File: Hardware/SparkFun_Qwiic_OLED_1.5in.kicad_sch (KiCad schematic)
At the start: 39 parts, among them J1 Qwiic_RA, J2 Qwiic_RA, J3 Conn_01x06, U1 OLED_1.5in, U5 AP3012

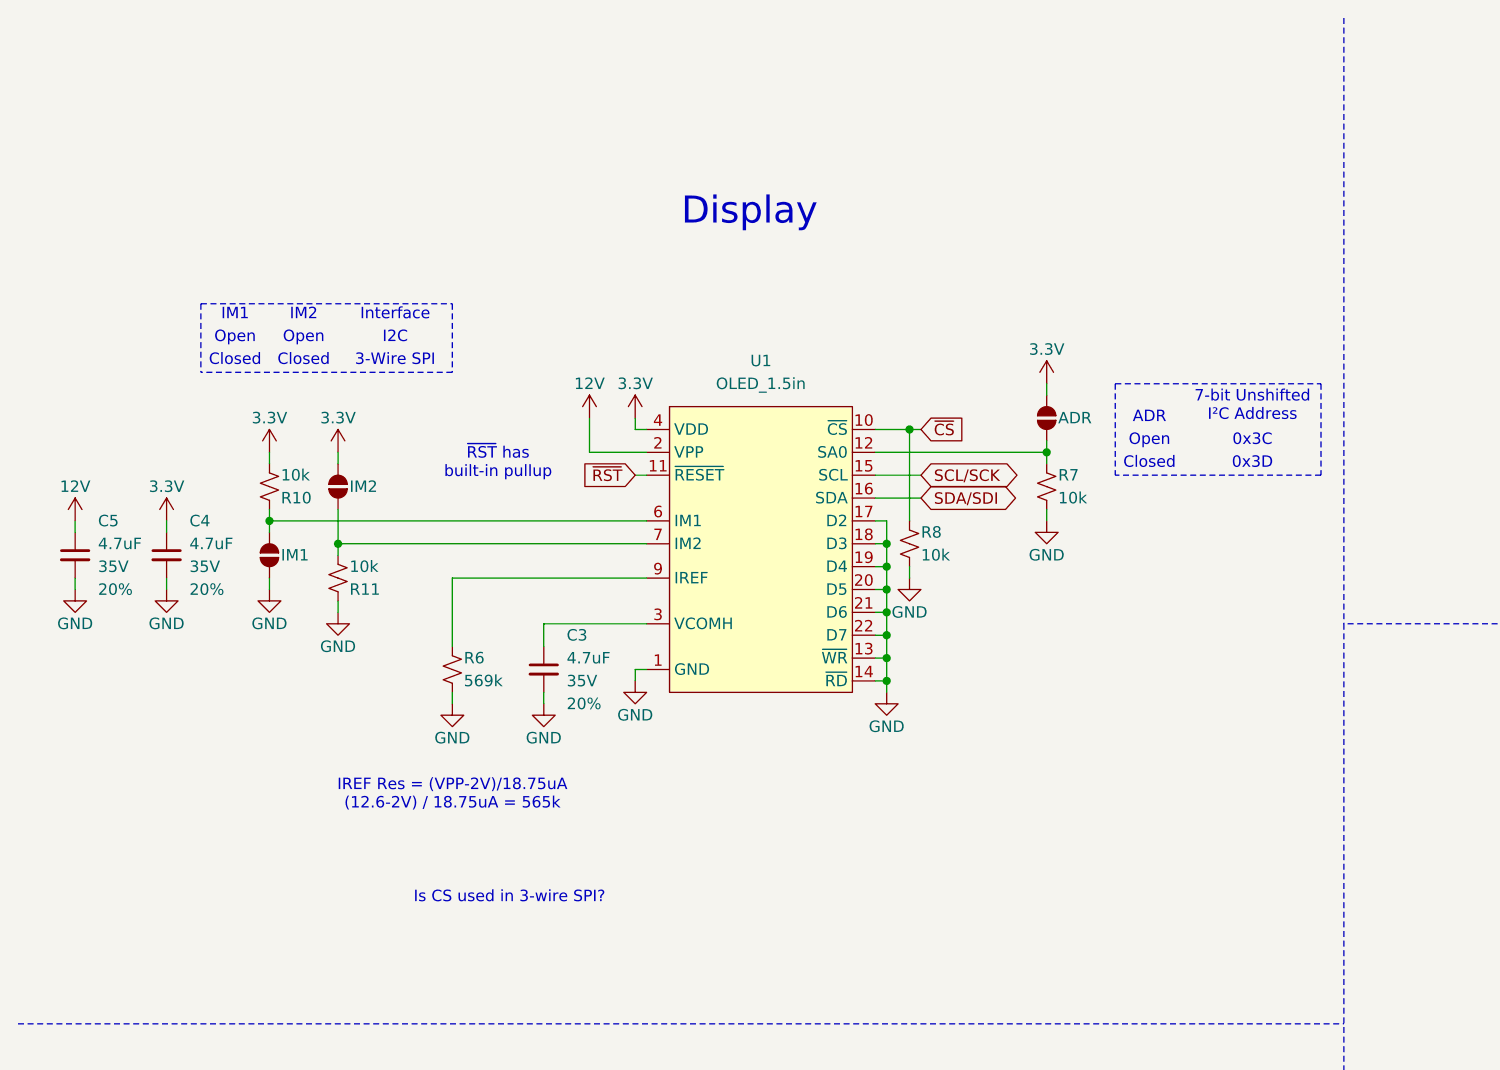
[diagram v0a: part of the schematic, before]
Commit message: Updates the display part to be it's own symbol
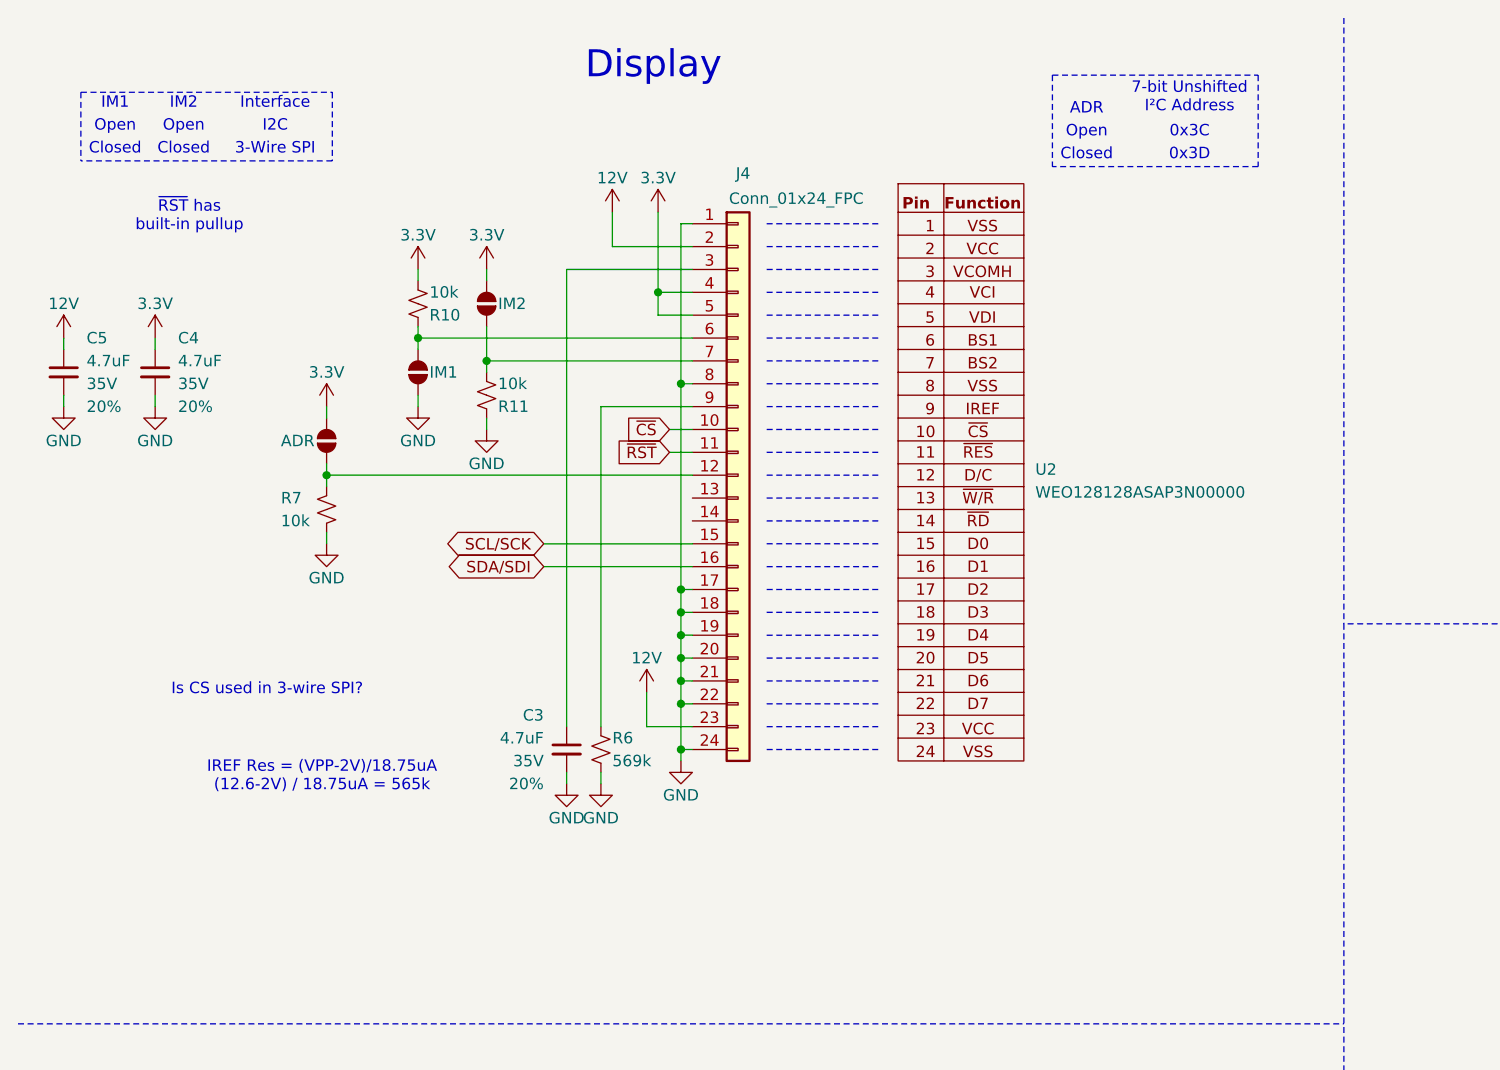
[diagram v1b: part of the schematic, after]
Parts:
- removed R8: 10k, SparkFun-Resistor:R_0603_1608Metric, symbol SparkFun-Resistor:10k_0603
- removed U1: OLED_1.5in, SparkFun-Display:OLED_1.5in_128x128-Folded, symbol SparkFun-Display:OLED_1.5in
- added J4: Conn_01x24_FPC, SparkFun-Connector:FPC_0.5mm-24, symbol SparkFun-Connector:Conn_01x24_FPC_0.5mm
- added U2: WEO128128ASAP3N00000, SparkFun-Display:OLED_1.5in_128x128-Folded, symbol SparkFun-Display:OLED_1.5in_New
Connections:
- net 12V: now also J4.2 (Pin_2), J4.23 (Pin_23)
- net 3.3V: now also J4.4 (Pin_4), J4.5 (Pin_5)
- net SCL/SCK: now also J4.15 (Pin_15)
- net SDA/SDI: now also J4.16 (Pin_16)
- net ~{CS}: now also J4.10 (Pin_10)
- net ~{RST}: now also J4.11 (Pin_11)
- net at JP6.2 (B), R10.2: now also J4.6 (Pin_6)
- net at R6.2: now also J4.9 (Pin_9)
- net at C3.1: now also J4.3 (Pin_3)
- net at JP3.1 (A), R7.2: now also J4.12 (Pin_12)
- net at JP7.1 (A), R11.1: now also J4.7 (Pin_7)
- net ESD_GND renamed GND
- net GND: now also J4.1 (Pin_1), J4.17 (Pin_17), J4.18 (Pin_18), J4.19 (Pin_19), J4.20 (Pin_20), J4.21 (Pin_21), J4.22 (Pin_22), J4.24 (Pin_24), J4.8 (Pin_8)
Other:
- moved on the sheet: C3, C4, C5, R10, R11, R6, R7

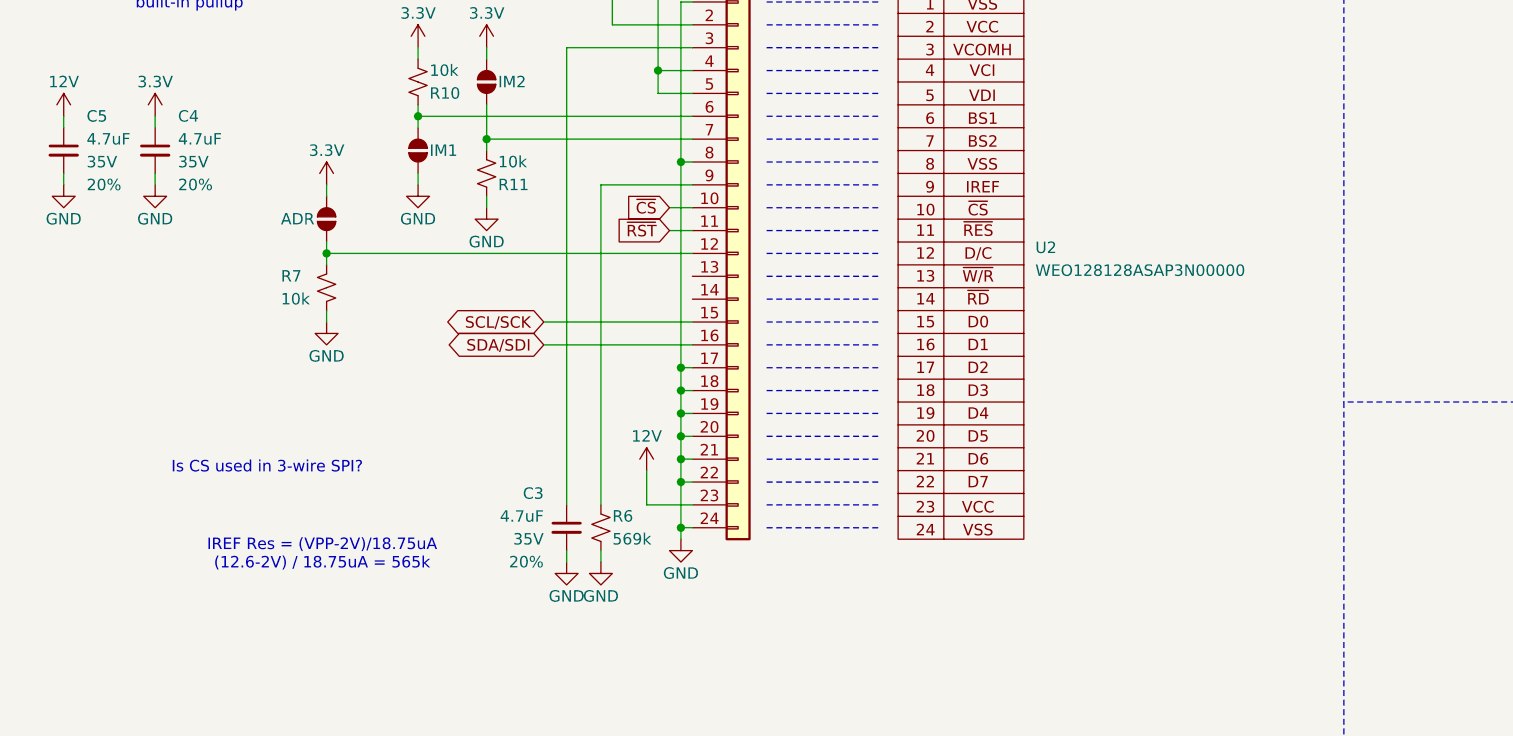
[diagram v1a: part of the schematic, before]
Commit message: Removes connector from OLED symbol
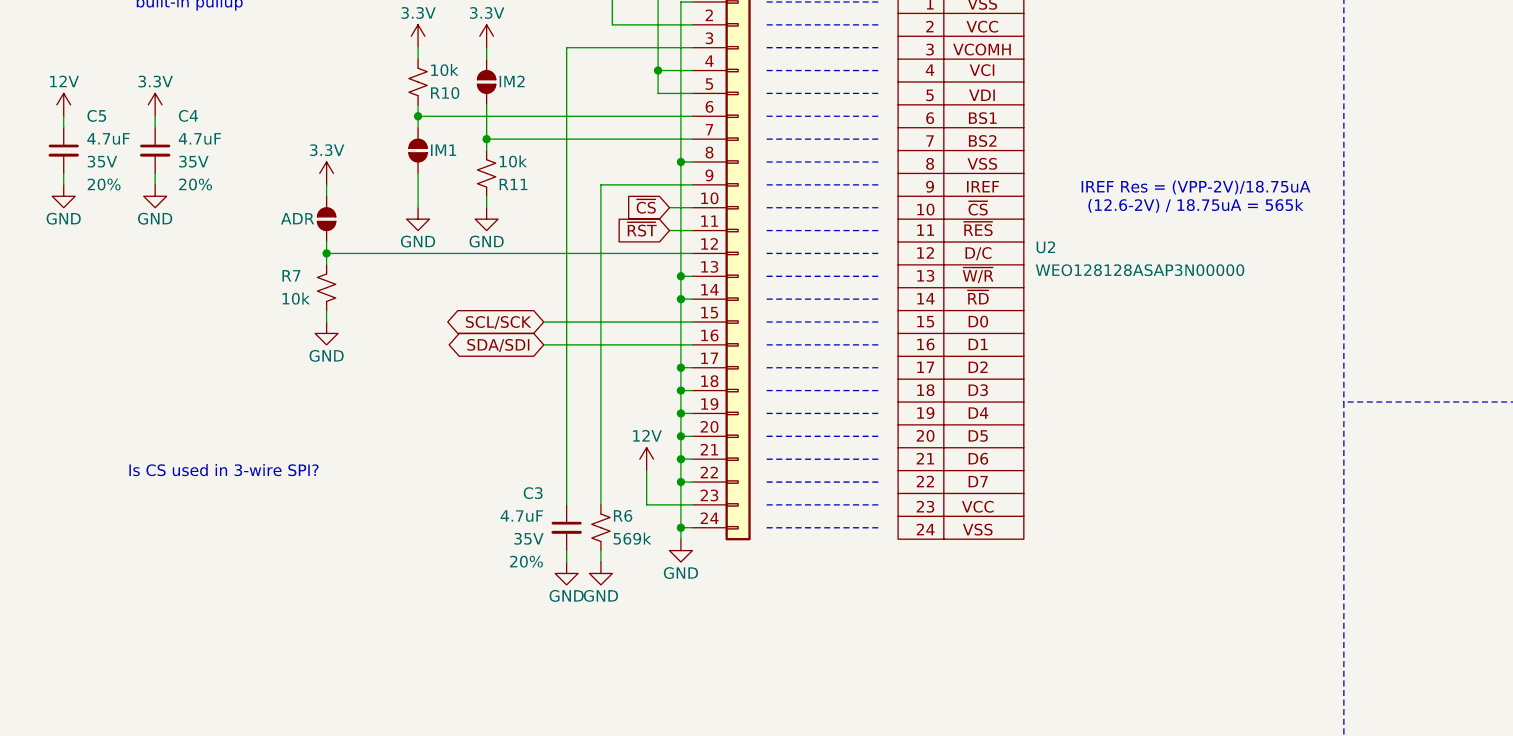
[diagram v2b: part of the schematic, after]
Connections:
- net GND: now also J4.13 (Pin_13), J4.14 (Pin_14)
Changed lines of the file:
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@@
 	(text "IREF Res = (VPP-2V)/18.75uA\n(12.6-2V) / 18.75uA = 565k"
 		(exclude_from_sim no)
-		(at 46.482 98.298 0)
+		(at 143.51 58.674 0)
 		(effects
 			(font
@@
 	(text "Is CS used in 3-wire SPI?"
 		(exclude_from_sim no)
-		(at 40.386 88.646 0)
+		(at 35.56 89.154 0)
 		(effects
 			(font
@@
 	)
 	(junction
+		(at 86.36 69.85)
+		(diameter 0)
+		(color 0 0 0 0)
+	)
+	(junction
 		(at 83.82 44.45)
 		(diameter 0)
@@
 	)
 	(junction
+		(at 86.36 67.31)
+		(diameter 0)
+		(color 0 0 0 0)
+	)
+	(junction
 		(at 46.99 64.77)
 		(diameter 0)
@@
 	(wire
 		(pts
+			(xy 86.36 67.31) (xy 86.36 69.85)
+		)
+		(stroke
+			(width 0)
+			(type default)
+		)
+	)
+	(wire
+		(pts
 			(xy 85.09 173.99) (xy 83.82 173.99)
 		)
@@
 		)
 	)
+	(wire
+		(pts
+			(xy 86.36 67.31) (xy 87.63 67.31)
+		)
+		(stroke
+			(width 0)
+			(type default)
+		)
+	)
 	(polyline
 		(pts
@@
 	(wire
 		(pts
+			(xy 86.36 69.85) (xy 87.63 69.85)
+		)
+		(stroke
+			(width 0)
+			(type default)
+		)
+	)
+	(wire
+		(pts
 			(xy 83.82 176.53) (xy 83.82 177.8)
 		)
@@
 	(wire
 		(pts
+			(xy 86.36 69.85) (xy 86.36 77.47)
+		)
+		(stroke
+			(width 0)
+			(type default)
+		)
+	)
+	(wire
+		(pts
 			(xy 57.15 48.26) (xy 57.15 49.53)
 		)
@@
 	(wire
 		(pts
-			(xy 57.15 57.15) (xy 57.15 55.88)
+			(xy 57.15 59.69) (xy 57.15 55.88)
 		)
 		(stroke
@@
 	(wire
 		(pts
-			(xy 86.36 54.61) (xy 86.36 77.47)
+			(xy 86.36 54.61) (xy 86.36 67.31)
 		)
 		(stroke
@@
 	(symbol
 		(lib_id "SparkFun-PowerSymbol:GND")
-		(at 57.15 57.15 0)
+		(at 57.15 59.69 0)
 		(unit 1)
 		(exclude_from_sim no)
@@
 		(fields_autoplaced yes)
 		(property "Reference" "#PWR02"
-			(at 57.15 63.5 0)
+			(at 57.15 66.04 0)
 			(effects
 				(font
@@
 		)
 		(property "Value" "GND"
-			(at 57.15 60.96 0)
+			(at 57.15 63.5 0)
 			(do_not_autoplace yes)
 			(effects
@@
 		)
 		(property "Footprint" ""
-			(at 57.15 57.15 0)
+			(at 57.15 59.69 0)
 			(effects
 				(font
@@
 		)
 		(property "Datasheet" ""
-			(at 57.15 57.15 0)
+			(at 57.15 59.69 0)
 			(effects
 				(font
@@
 		)
 		(property "Description" "Power symbol creates a global label with name \"GND\" , ground"
-			(at 57.15 66.04 0)
+			(at 57.15 68.58 0)
 			(effects
 				(font

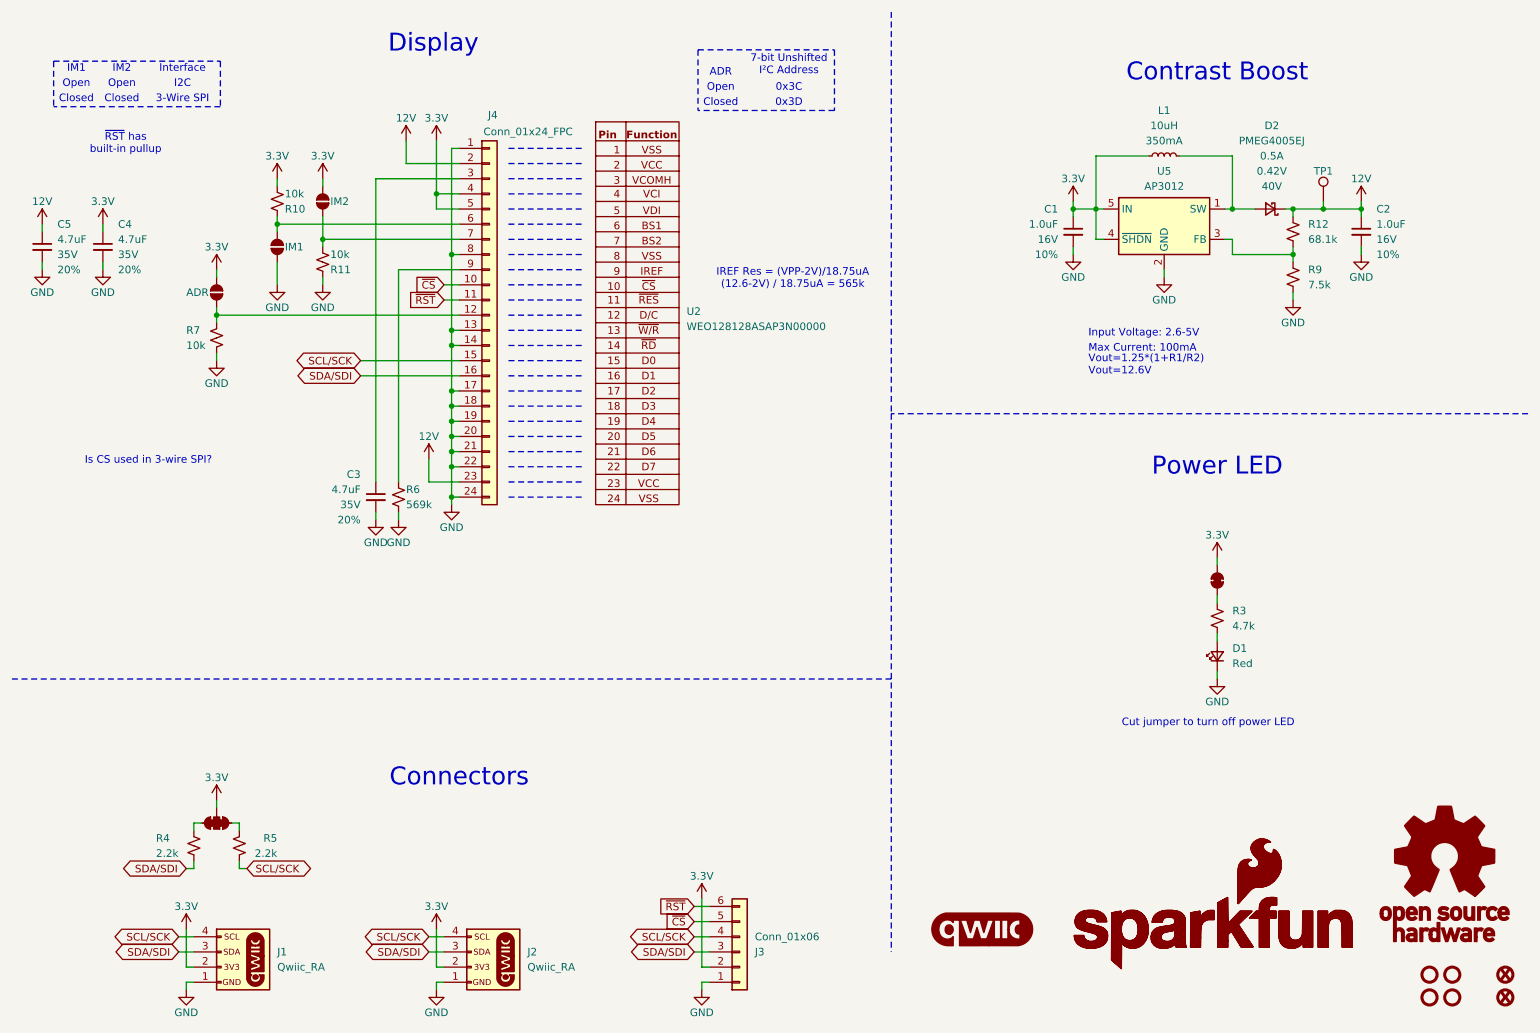
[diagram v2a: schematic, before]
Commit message: Removes connector from OLED symbolbol and footprint
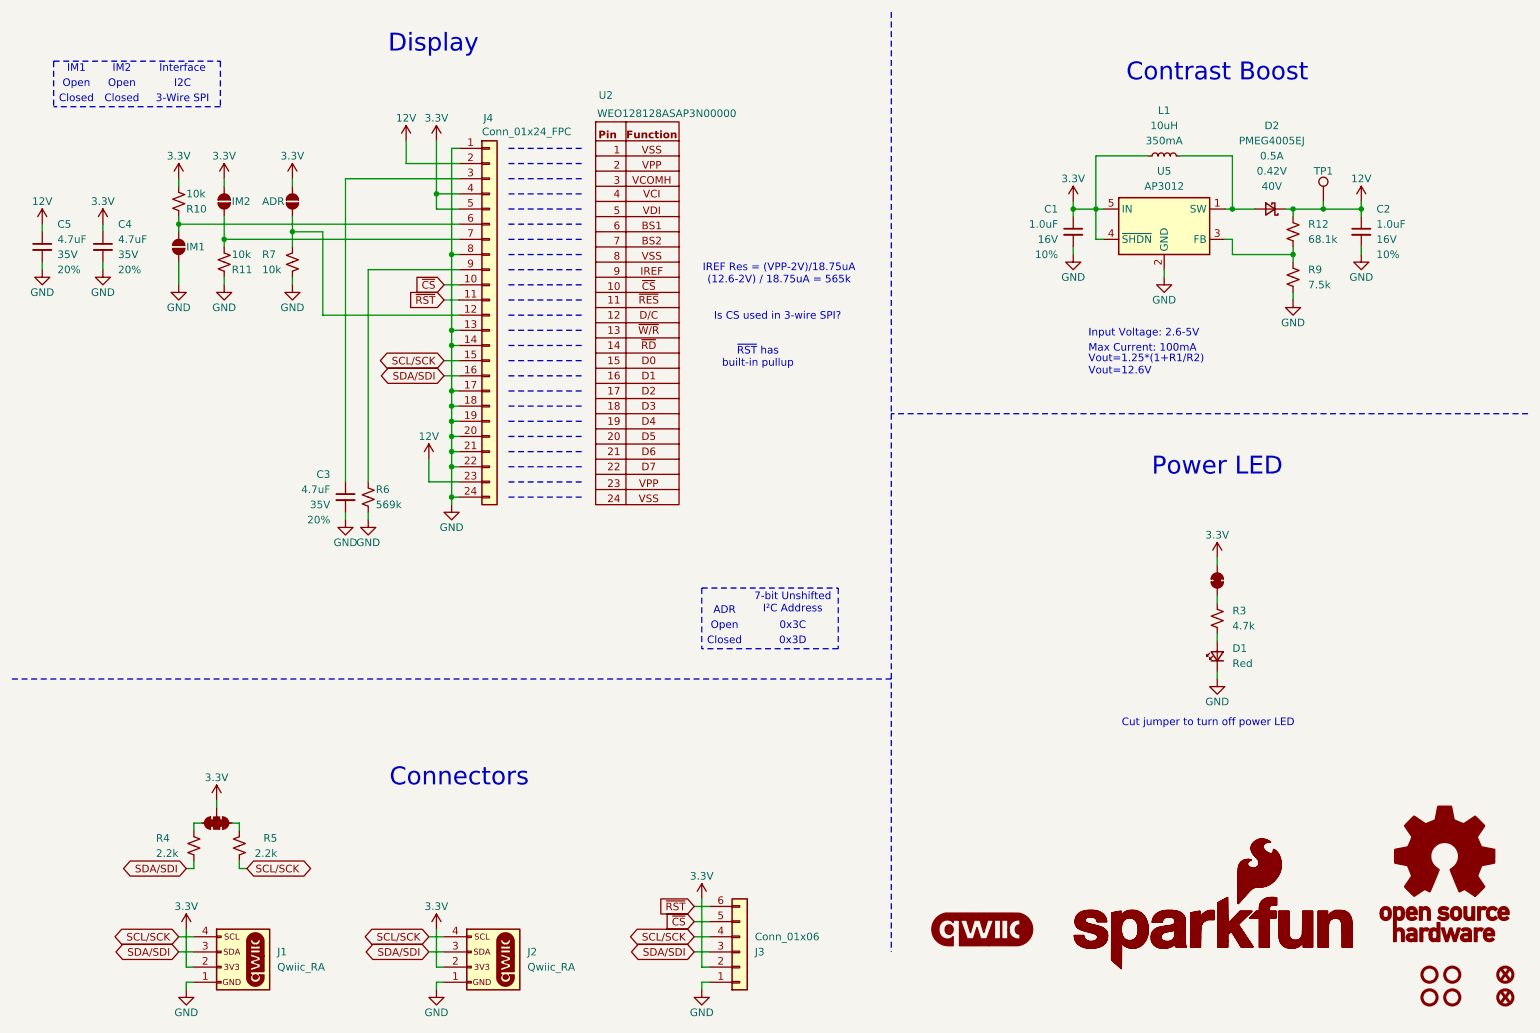
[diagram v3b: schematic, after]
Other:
- moved on the sheet: C3, R10, R11, R6, R7
